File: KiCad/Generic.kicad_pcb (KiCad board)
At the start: 2 copper layers, 19 x 29 mm, 40 parts, among them J1 Connector, J2 USB-C, J3 DC, Q1 RN1701, U1 ESP32-WROOM-32, U2 FT231XQ, U3 NX6020CAKS, U4 LMR16006YQ3

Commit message: Kicad 6
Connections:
- J2 pad A8: Net-(J2-PadA8) -> unconnected-(J2-PadA8)
- J2 pad B8: Net-(J2-PadB8) -> unconnected-(J2-PadB8)
- U1 pad 17: Net-(U1-Pad17) -> unconnected-(U1-Pad17)
- U1 pad 18: Net-(U1-Pad18) -> unconnected-(U1-Pad18)
- U1 pad 19: Net-(U1-Pad19) -> unconnected-(U1-Pad19)
- U1 pad 20: Net-(U1-Pad20) -> unconnected-(U1-Pad20)
- U1 pad 21: Net-(U1-Pad21) -> unconnected-(U1-Pad21)
- U1 pad 22: Net-(U1-Pad22) -> unconnected-(U1-Pad22)
- U1 pad 27: Net-(U1-Pad27) -> unconnected-(U1-Pad27)
- U1 pad 30: Net-(U1-Pad30) -> unconnected-(U1-Pad30)
- U1 pad 31: Net-(U1-Pad31) -> unconnected-(U1-Pad31)
- U1 pad 32: Net-(U1-Pad32) -> unconnected-(U1-Pad32)
- U1 pad 33: Net-(U1-Pad33) -> unconnected-(U1-Pad33)
- U1 pad 37: Net-(U1-Pad37) -> unconnected-(U1-Pad37)
- U1 pad 4: Net-(U1-Pad4) -> unconnected-(U1-Pad4)
- U1 pad 5: Net-(U1-Pad5) -> unconnected-(U1-Pad5)
- U2 pad 16: Net-(U2-Pad16) -> unconnected-(U2-Pad16)
- U2 pad 7: Net-(U2-Pad7) -> unconnected-(U2-Pad7)
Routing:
- net GND: track 161.7 -> 156.0 mm
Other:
- net class Default removed
- board text added: "${DATE}"
- board text removed: "2021-07-20"

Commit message: Tidy
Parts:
- turned L1 to 0 degrees

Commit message: Kicad 6
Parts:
- D3, D4: footprint Package_TO_SOT_SMD:SOT-363_SC-70-6 -> RevK:SOT-363_SC-70-6
- U1: footprint RevK:ESP32-WROOM-32 -> RF_Module:ESP32-WROOM-32

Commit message: Tidy
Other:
- board text removed: "V6"

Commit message: Curvy
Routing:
- net GND: track 156.0 -> 166.4 mm
- net +3V3: track 84.4 -> 82.1 mm
- net IO4: track 27.6 -> 28.8 mm
- net VBUS: track 14.8 -> 14.0 mm
- net DC: track 51.9 -> 51.3 mm

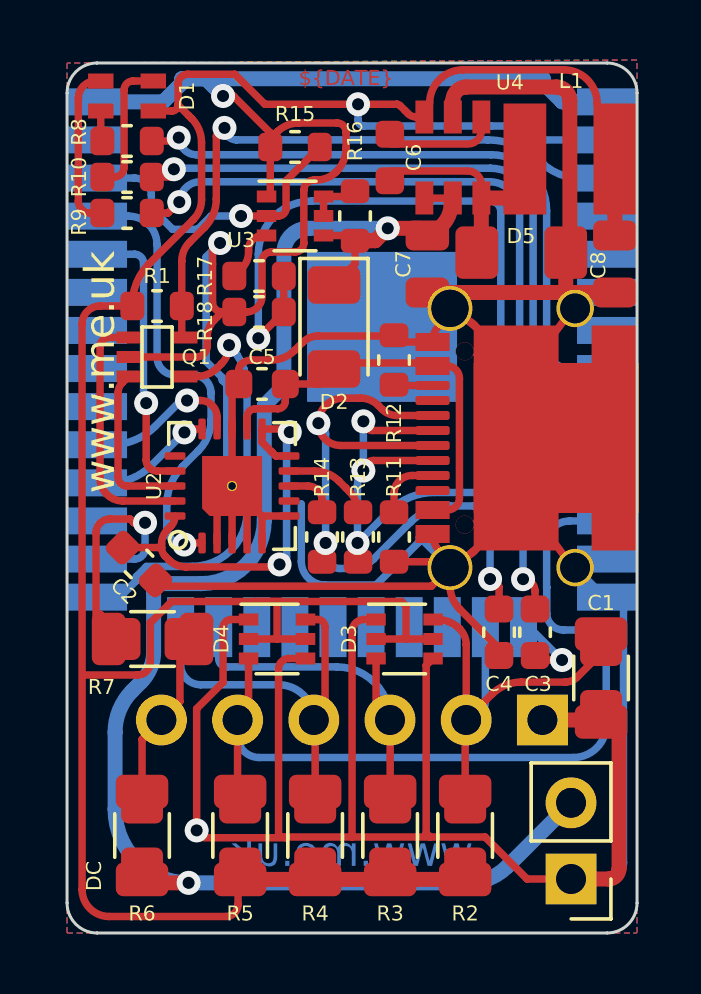
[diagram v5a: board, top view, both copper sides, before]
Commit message: Revised to allow for non fixed reg LMR16006 as more available
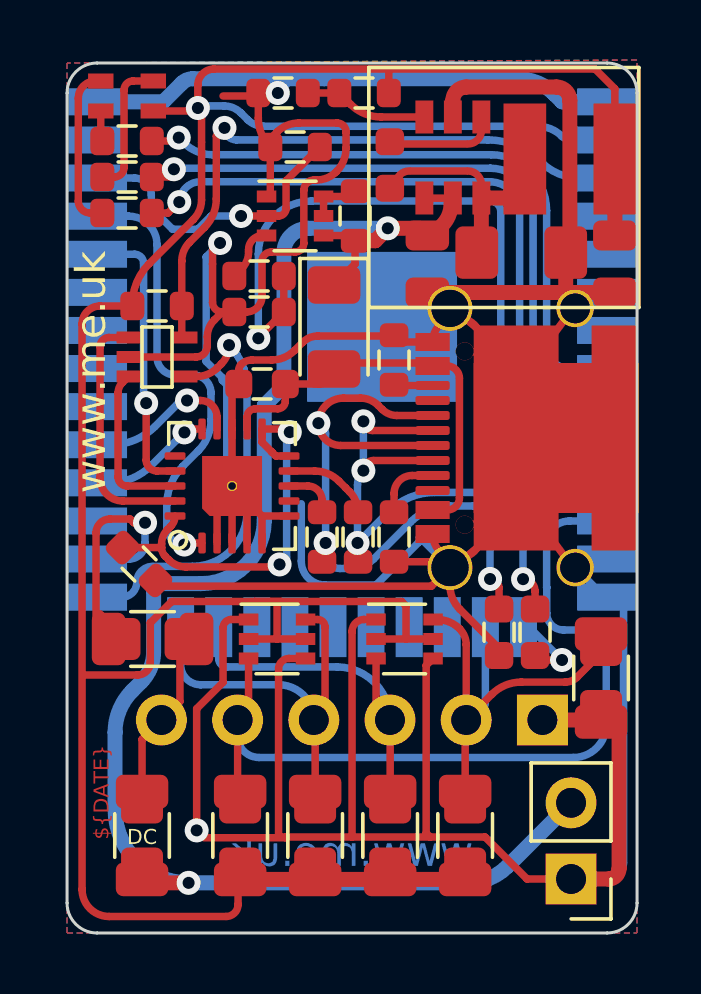
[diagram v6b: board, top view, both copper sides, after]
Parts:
- added R16: 10M 1% or 0R, RevK:R_0603, F.Cu at (127.1, 99.6)
- added R17: 3M 1% or NF, RevK:R_0603, F.Cu at (124.4, 99.6)
- U4: value LMR16006YQ3 -> LMR16006+FB; footprint RevK:RegulatorBlock -> RevK:RegulatorBlockFB
- moved C6 0.25 mm to (128.0, 102.0)
- renumbered R16 to R18, R17 to R19, R18 to R20
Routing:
- net +3V3: track 82.1 -> 96.0 mm
- net Net-(R16-Pad2): track 0.00 -> 4.15 mm
- net GND: track 166.4 -> 167.9 mm
